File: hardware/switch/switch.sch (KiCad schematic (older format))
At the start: 30 parts, among them J1 Conn_01x07, J2 Conn_01x04, J3 Conn_01x04, J4 Conn_01x04, K1 G6SU-2, K2 G6SU-2, K3 G6SU-2, K4 G6SU-2, SW1 D2F-01, SW2 D2F-01, SW3 D2F-01, SW4 D2F-01, U1 NCV7726B, U2 STM32F042F6Px, U3 SN65HVD230, U4 TPS82130

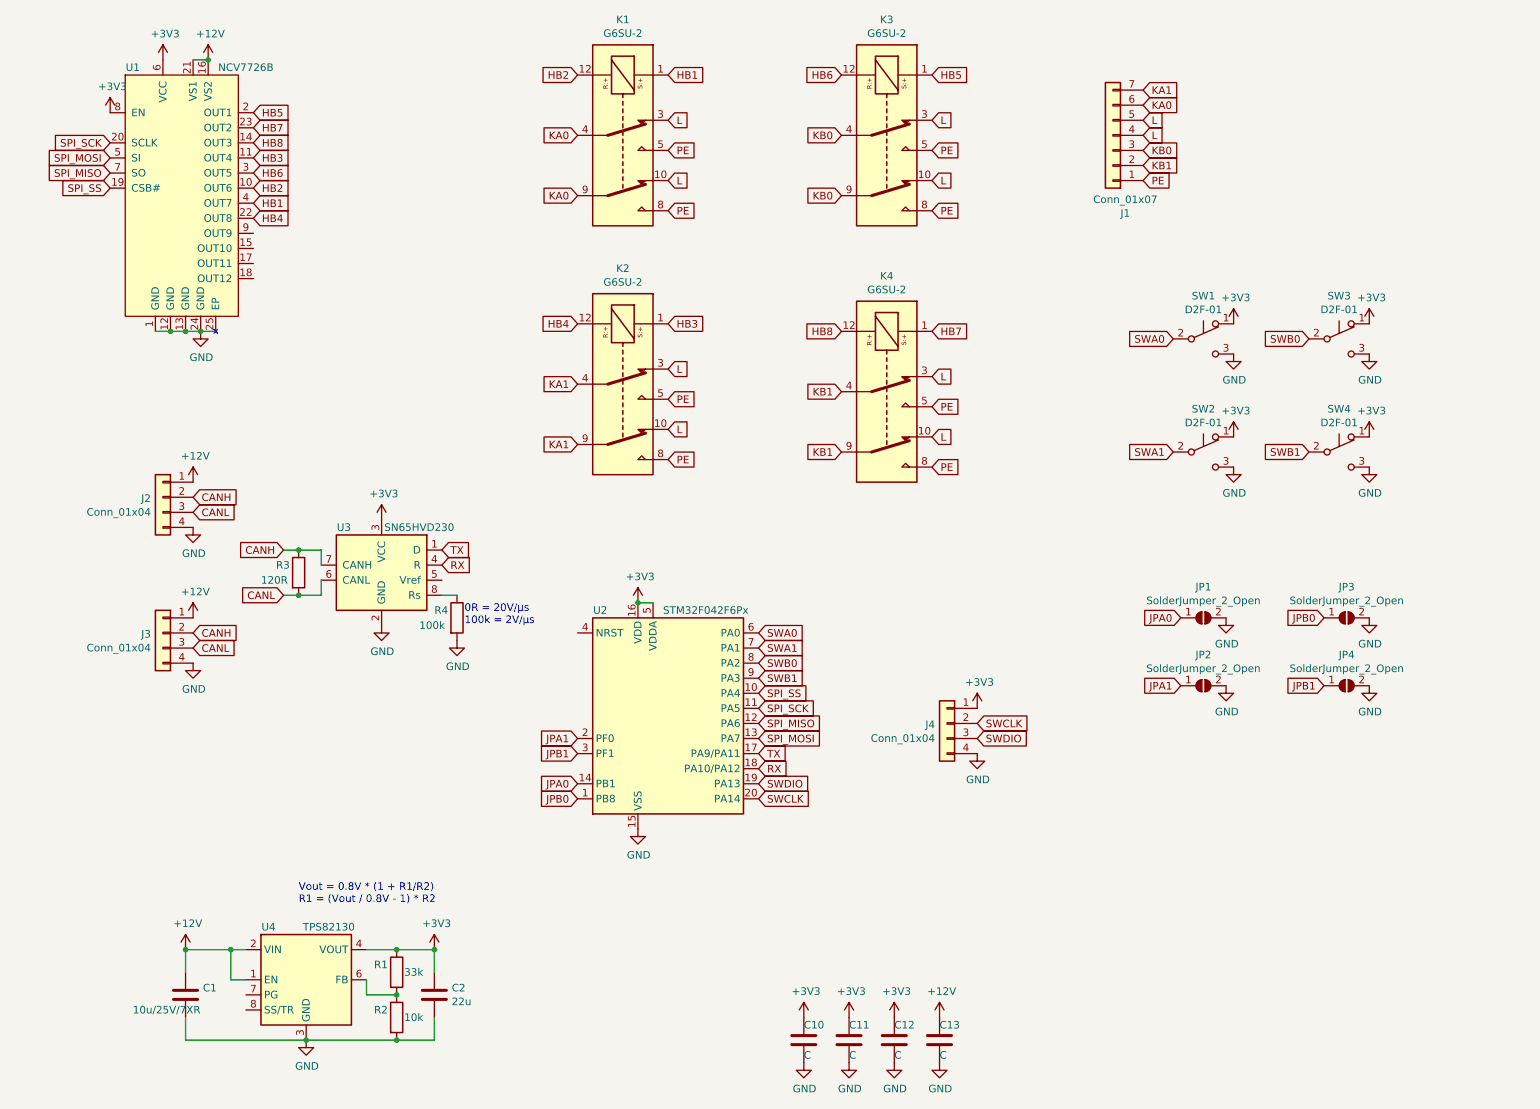
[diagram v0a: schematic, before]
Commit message: Use LIN instead of CAN transciever
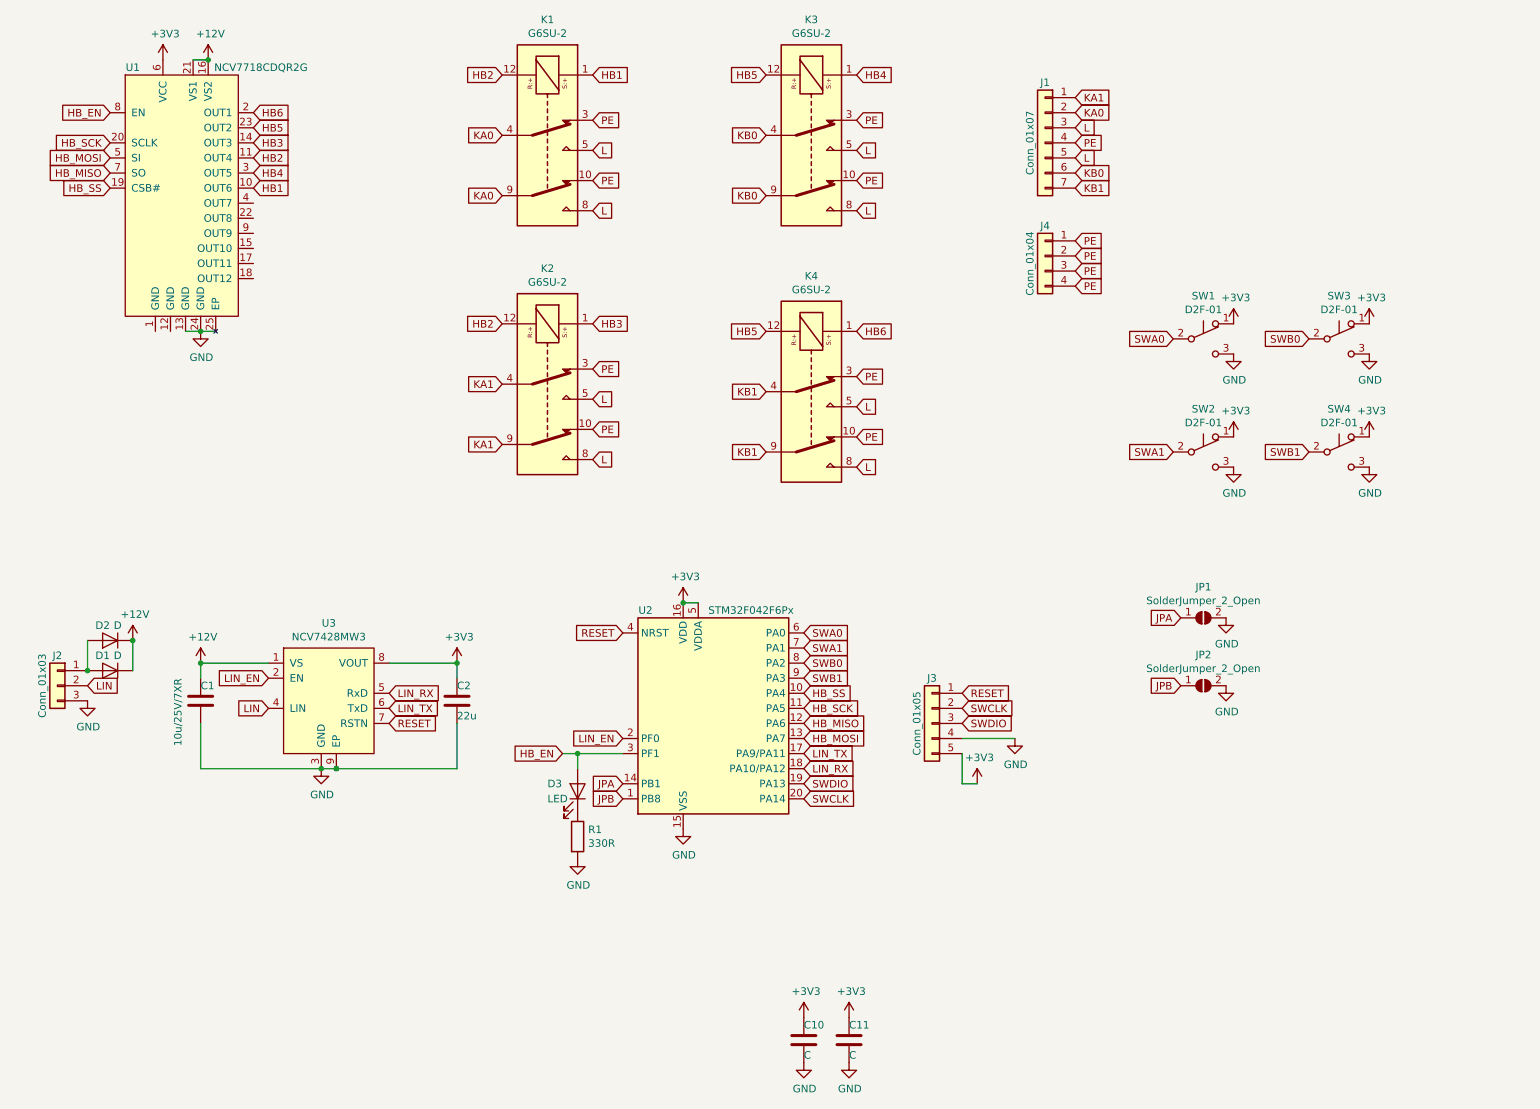
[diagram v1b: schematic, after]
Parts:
- removed C12, C13: C, Capacitor_SMD:C_0603_1608Metric, symbol Device:C
- removed J2, J3: Conn_01x04, Connector_PinHeader_2.54mm:PinHeader_1x04_P2.54mm_Vertical, symbol Connector_Generic:Conn_01x04
- removed JP3, JP4: SolderJumper_2_Open, Jumper:SolderJumper-2_P1.3mm_Open_TrianglePad1.0x1.5mm, symbol Jumper:SolderJumper_2_Open
- removed R2: 10k, Resistor_SMD:R_0603_1608Metric, symbol Device:R
- removed R3: 120R, Resistor_SMD:R_1206_3216Metric, symbol Device:R
- removed R4: 100k, Resistor_SMD:R_0603_1608Metric, symbol Device:R
- removed U1: NCV7726B, RoomControl:On_NCV7726B, symbol RoomControl:NCV7726B
- removed U3: SN65HVD230, Package_SO:SOIC-8_3.9x4.9mm_P1.27mm, symbol Interface_CAN_LIN:SN65HVD230
- removed U4: TPS82130, RoomControl:Texas_TPS82130, symbol Regulator_Switching:TPS82130
- added D1: D, Diode_SMD:D_1206_3216Metric_Castellated, symbol Device:D
- added D2: D, Diode_SMD:D_SOT-23_ANK, symbol Device:D
- added D3: LED, LED_SMD:LED_0805_2012Metric_Castellated, symbol Device:LED
- added J2: Conn_01x03, RoomControl:Wago_236-403, symbol Connector_Generic:Conn_01x03
- added J3: Conn_01x05, Connector_PinHeader_2.54mm:PinHeader_1x05_P2.54mm_Vertical, symbol Connector_Generic:Conn_01x05
- added U1: NCV7718CDQR2G, RoomControl:On_NCV77xx, symbol RoomControl:NCV77xx
- added U3: NCV7428MW3, Package_DFN_QFN:DFN-8-1EP_3x3mm_P0.65mm_EP1.55x2.4mm, symbol RoomControl:NCV7428MW
- J4: footprint Connector_PinHeader_2.54mm:PinHeader_1x04_P2.54mm_Vertical -> RoomControl:Switch_Mount
- R1: value 33k -> 330R
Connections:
- net HB7 is gone; now on net HB6: K4.1
- net HB8 is gone; now on net HB5: K4.12
- net JPB0 is gone; now on net JPB: U2.1 (PB8)
- net +12V: now also D1.1 (K), D2.1 (K), U1.16 (VS2), U1.21 (VS1), U3.1 (VS)
- net +3V3: now also J3.5 (Pin_5), U1.6 (VCC), U3.8 (VOUT); no longer J4.1 (Pin_1), R1.1
- net GND: now also R1.2, J2.3 (Pin_3), J3.4 (Pin_4), U1.13 (GND), U1.24 (GND), U1.25 (EP), U3.3 (GND), U3.9 (EP); no longer J4.4 (Pin_4)
- net HB1: now also U1.10 (OUT6)
- net HB2: now also K2.12, U1.11 (OUT4)
- net HB3: now also U1.14 (OUT3)
- net HB4: now also K3.1, U1.3 (OUT5); no longer K2.12
- net HB5: now also K3.12, U1.23 (OUT2); no longer K3.1
- net HB6: now also U1.2 (OUT1); no longer K3.12
- net KA0: now also J1.2 (Pin_2); no longer J1.6 (Pin_6)
- net KA1: now also J1.1 (Pin_1); no longer J1.7 (Pin_7)
- net KB0: now also J1.6 (Pin_6); no longer J1.3 (Pin_3)
- net KB1: now also J1.7 (Pin_7); no longer J1.2 (Pin_2)
- net L: now also J1.3 (Pin_3), K1.5, K1.8, K2.5, K2.8, K3.5, K3.8, K4.5, K4.8; no longer J1.4 (Pin_4), K1.10, K1.3, K2.10, K2.3, K3.10, K3.3, K4.10, K4.3
- net PE: now also J1.4 (Pin_4), J4.1 (Pin_1), J4.2 (Pin_2), J4.3 (Pin_3), J4.4 (Pin_4), K1.10, K1.3, K2.10, K2.3, K3.10, K3.3, K4.10, K4.3; no longer J1.1 (Pin_1), K1.5, K1.8, K2.5, K2.8, K3.5, K3.8, K4.5, K4.8
- net SWCLK: now also J3.2 (Pin_2); no longer J4.2 (Pin_2)
- net SWDIO: now also J3.3 (Pin_3); no longer J4.3 (Pin_3)
- net RESET: now reaches U2.4 (NRST)
- net RESET: now also J3.1 (Pin_1), U3.7 (RSTN)
- net JPA0 renamed JPA
- net JPA1 renamed JPB
- net JPB: no longer U2.2 (PF0)
- net JPB1 renamed HB_EN
- net HB_EN: now also D3.2 (A), U1.8 (EN)
- net RX renamed LIN_RX
- net LIN_RX: now also U3.5 (RxD)
- net SPI_MISO renamed HB_MISO
- net HB_MISO: now also U1.7 (SO)
- net SPI_MOSI renamed HB_MOSI
- net HB_MOSI: now also U1.5 (SI)
- net SPI_SCK renamed HB_SCK
- net HB_SCK: now also U1.20 (SCLK)
- net SPI_SS renamed HB_SS
- net HB_SS: now also U1.19 (CSB#)
- net TX renamed LIN_TX
- net LIN_TX: now also U3.6 (TxD)
- new net: D1.2 (A), D2.2 (A), J2.1 (Pin_1)
- new net: D3.1 (K), R1.1
- new net LIN: J2.2 (Pin_2), U3.4 (LIN)
- new net LIN_EN: U2.2 (PF0), U3.2 (EN)
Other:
- note removed: "0R = 20V/μs\n100k = 2V/μs"
- note removed: "Vout = 0.8V * (1 + R1/R2)\nR1 = (Vout / 0.8V - 1) * R2"
- moved on the sheet: J1, K1, K2, K3, K4, U2

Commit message: Update main board to use LIN
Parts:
- added D4: LED, LED_SMD:LED_0805_2012Metric_Castellated, symbol Device:LED
- added R2: 330R, Resistor_SMD:R_0603_1608Metric, symbol Device:R
- JP1, JP2: footprint Jumper:SolderJumper-2_P1.3mm_Open_TrianglePad1.0x1.5mm -> RoomControl:Jumper2Triangular
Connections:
- net +3V3: now also J3.4 (Pin_4); no longer J3.5 (Pin_5)
- net GND: now also J3.5 (Pin_5), R2.2; no longer J3.4 (Pin_4)
- net HB_EN: now also D4.2 (A); no longer D3.2 (A)
- net LIN: now also J2.1 (Pin_1); no longer J2.2 (Pin_2)
- net LIN_EN: now also D3.2 (A)
- net at D1.2 (A), D2.2 (A): now also J2.2 (Pin_2); no longer J2.1 (Pin_1)
- net HB1 renamed AX
- net HB2 renamed AY
- net HB3 renamed AZ
- net HB4 renamed BX
- net HB5 renamed BY
- net HB6 renamed BZ
- new net: D4.1 (K), R2.1
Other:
- moved on the sheet: C1, C2, D1, D2, D3, J3, JP1, JP2, R1, SW1, SW2, SW3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

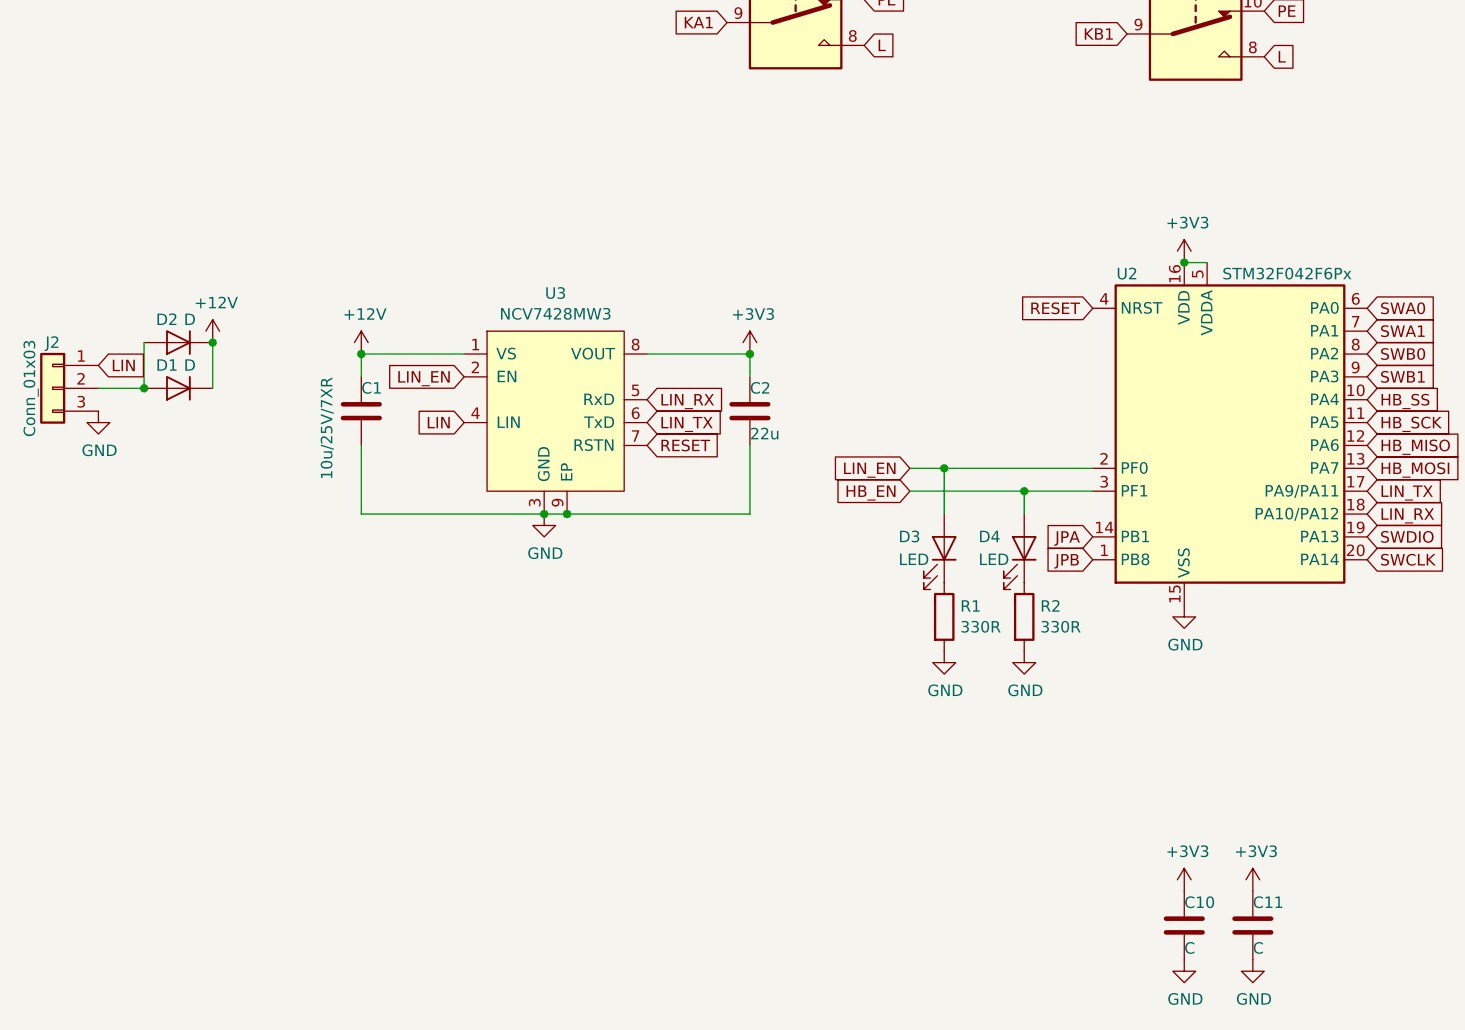
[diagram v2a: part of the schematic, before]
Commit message: Add backup battery and 32768Hz crystal
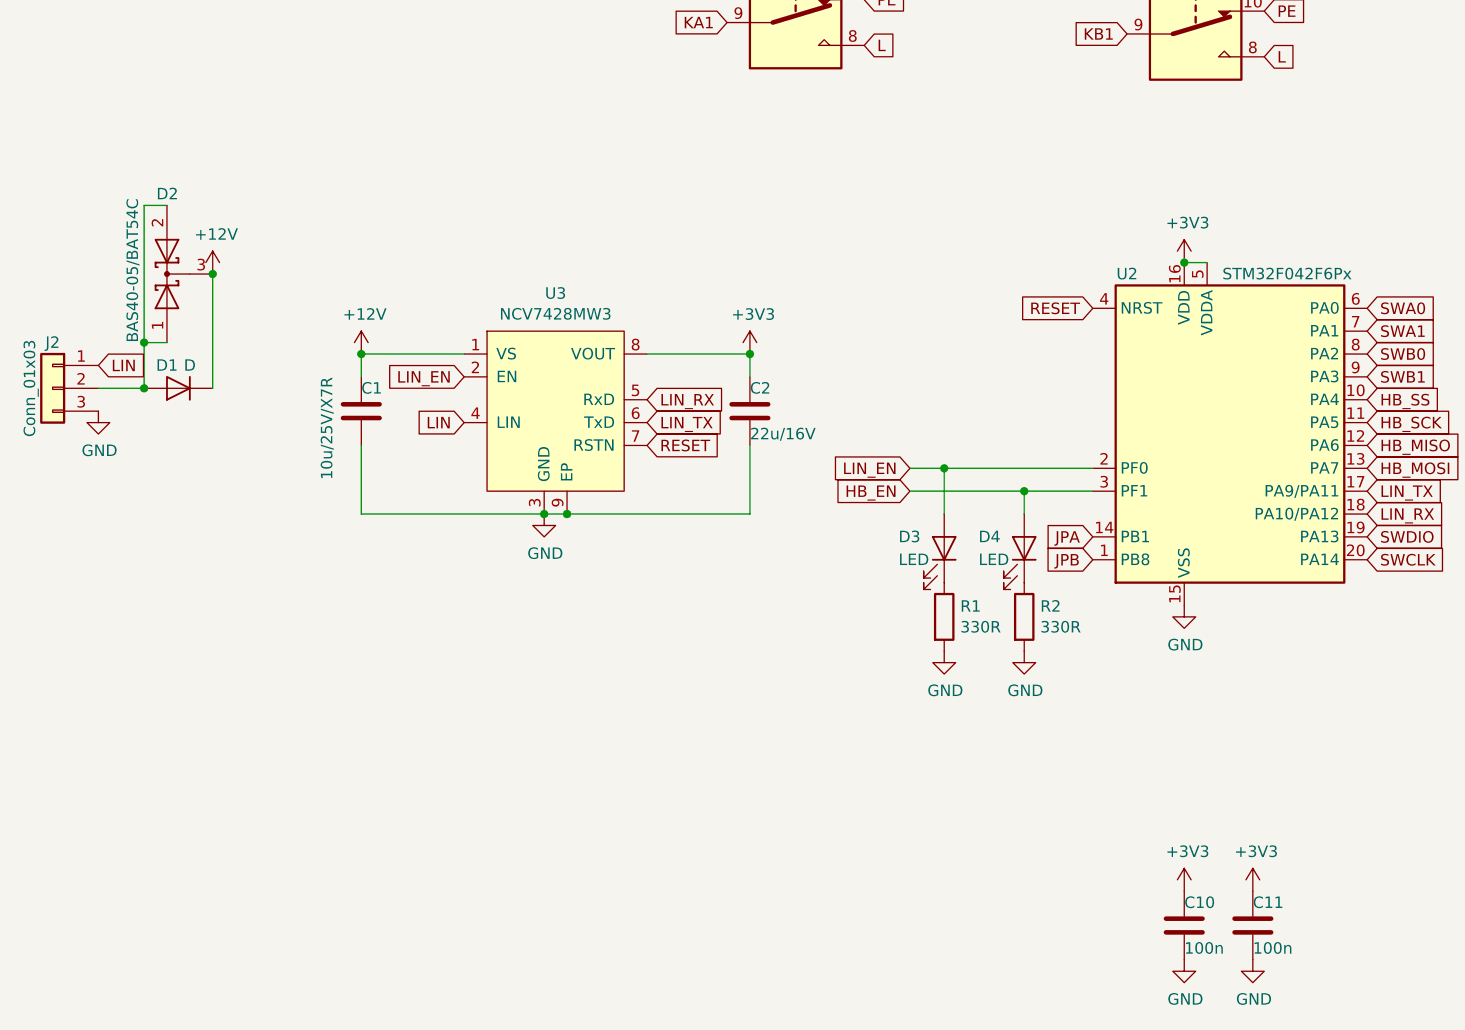
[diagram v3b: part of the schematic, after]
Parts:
- removed D2: D, Diode_SMD:D_SOT-23_ANK, symbol Device:D
- added D2: BAS40-05/BAT54C, Package_TO_SOT_SMD:SOT-23, symbol Device:D_Schottky_x2_KCom_AAK
- C1: value 10u/25V/7XR -> 10u/25V/X7R
- C10, C11: value C -> 100n
- C2: value 22u -> 22u/16V
- JP1, JP2: footprint RoomControl:Jumper2Triangular -> RoomControl:Jumper2
- U2: footprint Package_SO:TSSOP-20_4.4x6.5mm_P0.65mm -> RoomControl:STM32F042F6
- U3: footprint Package_DFN_QFN:DFN-8-1EP_3x3mm_P0.65mm_EP1.55x2.4mm -> RoomControl:On_NCV7428MW
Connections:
- net +12V: now also D2.3 (K)
- net at D1.2 (A), J2.2 (Pin_2): now also D2.1 (A), D2.2 (A)
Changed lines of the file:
@@
 F 0 "U2" H 5500 5800 50  0000 C CNN
 F 1 "STM32F042F6Px" H 6200 5800 50  0000 C CNN
-F 2 "Package_SO:TSSOP-20_4.4x6.5mm_P0.65mm" H 5450 4450 50  0001 R CNN
+F 2 "RoomControl:STM32F042F6" H 5450 4450 50  0001 R CNN
 F 3 "http://www.st.com/st-web-ui/static/active/en/resource/technical/document/datasheet/DM00105814.pdf" H 5950 5150 50  0001 C CNN
 	1    5950 5150
@@
 L power:+12V #PWR0121
 U 1 1 5EC5C5A0
-P 1500 4800
-F 0 "#PWR0121" H 1500 4650 50  0001 C CNN
-F 1 "+12V" H 1515 4973 50  0000 C CNN
-F 2 "" H 1500 4800 50  0001 C CNN
-F 3 "" H 1500 4800 50  0001 C CNN
-	1    1500 4800
+P 1500 4500
+F 0 "#PWR0121" H 1500 4350 50  0001 C CNN
+F 1 "+12V" H 1515 4673 50  0000 C CNN
+F 2 "" H 1500 4500 50  0001 C CNN
+F 3 "" H 1500 4500 50  0001 C CNN
+	1    1500 4500
 	1    0    0    -1
 $EndComp
@@
 P 5750 7350
 F 0 "C10" H 5750 7450 50  0000 L CNN
-F 1 "C" H 5750 7250 50  0000 L CNN
+F 1 "100n" H 5750 7250 50  0000 L CNN
 F 2 "Capacitor_SMD:C_0603_1608Metric" H 5788 7200 50  0001 C CNN
 F 3 "~" H 5750 7350 50  0001 C CNN
@@
 P 6050 7350
 F 0 "C11" H 6050 7450 50  0000 L CNN
-F 1 "C" H 6050 7250 50  0000 L CNN
+F 1 "100n" H 6050 7250 50  0000 L CNN
 F 2 "Capacitor_SMD:C_0603_1608Metric" H 6088 7200 50  0001 C CNN
 F 3 "~" H 6050 7350 50  0001 C CNN
@@
 F 0 "JP1" H 9200 4755 50  0000 C CNN
 F 1 "SolderJumper_2_Open" H 9200 4664 50  0000 C CNN
-F 2 "RoomControl:Jumper2Triangular" H 9200 4550 50  0001 C CNN
+F 2 "RoomControl:Jumper2" H 9200 4550 50  0001 C CNN
 F 3 "~" H 9200 4550 50  0001 C CNN
 	1    9200 4550
@@
 F 0 "JP2" H 9200 5205 50  0000 C CNN
 F 1 "SolderJumper_2_Open" H 9200 5114 50  0000 C CNN
-F 2 "RoomControl:Jumper2Triangular" H 9200 5000 50  0001 C CNN
+F 2 "RoomControl:Jumper2" H 9200 5000 50  0001 C CNN
 F 3 "~" H 9200 5000 50  0001 C CNN
 	1    9200 5000
@@
 P 2150 5100
 F 0 "C1" H 2150 5200 50  0000 L CNN
-F 1 "10u/25V/7XR" V 2000 4800 50  0000 L CNN
+F 1 "10u/25V/X7R" V 2000 4800 50  0000 L CNN
 F 2 "Capacitor_SMD:C_1206_3216Metric" H 2188 4950 50  0001 C CNN
 F 3 "~" H 2150 5100 50  0001 C CNN
@@
 P 3850 5100
 F 0 "C2" H 3850 5200 50  0000 L CNN
-F 1 "22u" H 3850 5000 50  0000 L CNN
+F 1 "22u/16V" H 3850 5000 50  0000 L CNN
 F 2 "Capacitor_SMD:C_0805_2012Metric" H 3888 4950 50  0001 C CNN
 F 3 "~" H 3850 5100 50  0001 C CNN
@@
 F 0 "U3" H 3000 5715 50  0000 C CNN
 F 1 "NCV7428MW3" H 3000 5624 50  0000 C CNN
-F 2 "Package_DFN_QFN:DFN-8-1EP_3x3mm_P0.65mm_EP1.55x2.4mm" H 3000 5150 50  0001 C CNN
+F 2 "RoomControl:On_NCV7428MW" H 3000 5150 50  0001 C CNN
 F 3 "" H 3000 5150 50  0001 C CNN
 	1    3000 5150
@@
 Text GLabel 5350 4650 0    50   Input ~ 0
 RESET
-$Comp
-L Device:D D2
-U 1 1 5EE4724C
-P 1350 4800
-F 0 "D2" H 1400 4700 50  0000 C CNN
-F 1 "D" H 1300 4700 50  0000 C CNN
-F 2 "Diode_SMD:D_SOT-23_ANK" H 1350 4800 50  0001 C CNN
-F 3 "~" H 1350 4800 50  0001 C CNN
-	1    1350 4800
-	-1   0    0    1
-$EndComp
-Wire Wire Line
-	1500 5000 1500 4800
-Connection ~ 1500 4800
 Wire Wire Line
 	1000 5000 1200 5000
@@
 Wire Wire Line
 	4700 5350 5350 5350
+$Comp
+L Device:D_Schottky_x2_KCom_AAK D2
+U 1 1 5F27B92A
+P 1300 4500
+F 0 "D2" V 1650 4450 50  0000 L CNN
+F 1 "BAS40-05/BAT54C" H 1000 4650 50  0000 L CNN
+F 2 "Package_TO_SOT_SMD:SOT-23" H 1300 4500 50  0001 C CNN
+F 3 "~" H 1300 4500 50  0001 C CNN
+	1    1300 4500
+	0    -1   -1   0
+$EndComp
+Wire Wire Line
+	1500 4500 1500 5000
+Connection ~ 1500 4500
+Wire Wire Line
+	1200 4800 1300 4800
+Wire Wire Line
+	1200 4800 1200 4200
+Wire Wire Line
+	1200 4200 1300 4200
+Connection ~ 1200 4800
 $EndSCHEMATC
